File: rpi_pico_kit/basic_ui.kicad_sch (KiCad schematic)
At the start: 40 parts, among them SW2 RotaryEncoder_Switch, SW3 SW_Push, SW4 SW_Push, SW5 SW_Push, SW6 SW_Push, U11 74HC14, U5 74HC14

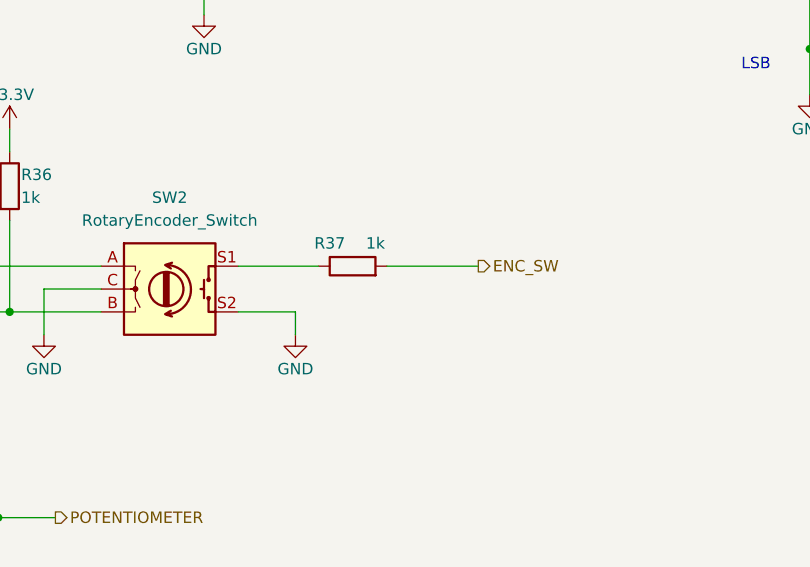
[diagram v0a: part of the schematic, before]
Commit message: changed encoder button pull-up to pull-down
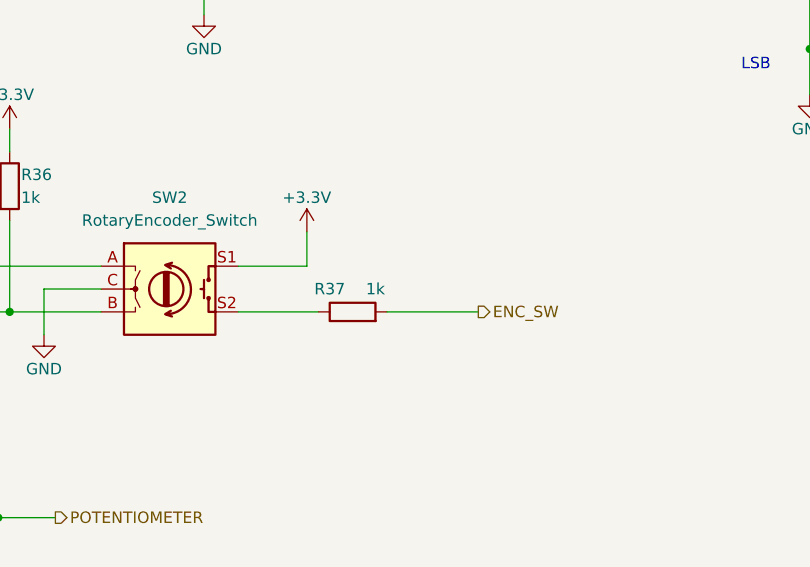
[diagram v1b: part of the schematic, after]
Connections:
- net +3V3: now also SW2.S1
- net GND: no longer SW2.S2
- net at R37.1: now also SW2.S2; no longer SW2.S1
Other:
- moved on the sheet: R37
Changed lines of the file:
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@@
+    (stroke (width 0) (type default))
+  )
+  (wire (pts (xy 92.71 142.24) (xy 92.71 138.43))
     (stroke (width 0) (type default))
   )
@@
     (stroke (width 0) (type default))
   )
-  (wire (pts (xy 85.09 142.24) (xy 93.98 142.24))
-    (stroke (width 0) (type default))
-  )
   (wire (pts (xy 227.33 129.54) (xy 227.33 130.81))
     (stroke (width 0) (type default))
@@
     (stroke (width 0) (type default))
   )
-  (wire (pts (xy 91.44 147.32) (xy 91.44 149.86))
-    (stroke (width 0) (type default))
-  )
   (wire (pts (xy 240.03 92.71) (xy 240.03 121.92))
     (stroke (width 0) (type default))
@@
     (stroke (width 0) (type default))
   )
+  (wire (pts (xy 85.09 142.24) (xy 92.71 142.24))
+    (stroke (width 0) (type default))
+  )
   (wire (pts (xy 48.26 147.32) (xy 59.69 147.32))
     (stroke (width 0) (type default))
@@
     (stroke (width 0) (type default))
   )
-  (wire (pts (xy 85.09 147.32) (xy 91.44 147.32))
-    (stroke (width 0) (type default))
-  )
   (wire (pts (xy 63.5 144.78) (xy 63.5 149.86))
     (stroke (width 0) (type default))
@@
     (stroke (width 0) (type default))
   )
+  (wire (pts (xy 85.09 147.32) (xy 93.98 147.32))
+    (stroke (width 0) (type default))
+  )
   (wire (pts (xy 101.6 99.06) (xy 101.6 101.6))
     (stroke (width 0) (type default))
@@
     (stroke (width 0) (type default))
   )
-  (wire (pts (xy 101.6 142.24) (xy 111.76 142.24))
+  (wire (pts (xy 101.6 147.32) (xy 111.76 147.32))
     (stroke (width 0) (type default))
   )
@@
     (effects (font (size 1.27 1.27)) (justify right))
   )
-  (hierarchical_label "ENC_SW" (shape output) (at 111.76 142.24 0) (fields_autoplaced)
+  (hierarchical_label "ENC_SW" (shape output) (at 111.76 147.32 0) (fields_autoplaced)
     (effects (font (size 1.27 1.27)) (justify left))
   )
@@
     (pin "2")
   )
-  (symbol (lib_id "power:GND") (at 91.44 149.86 0) (unit 1)
-    (in_bom yes) (on_board yes)
-    (property "Reference" "#PWR056" (id 0) (at 91.44 156.21 0)
-      (effects (font (size 1.27 1.27)) hide)
-    )
-    (property "Value" "GND" (id 1) (at 91.44 153.67 0)
-      (effects (font (size 1.27 1.27)))
-    )
-    (property "Footprint" "" (id 2) (at 91.44 149.86 0)
-      (effects (font (size 1.27 1.27)) hide)
-    )
-    (property "Datasheet" "" (id 3) (at 91.44 149.86 0)
-      (effects (font (size 1.27 1.27)) hide)
-    )
-    (pin "1")
-  )
   (symbol (lib_id "power:+3.3V") (at 59.69 127 0) (unit 1)
     (in_bom yes) (on_board yes)
@@
     (pin "2")
   )
-  (symbol (lib_id "Device:R") (at 97.79 142.24 90) (unit 1)
-    (in_bom yes) (on_board yes)
-    (property "Reference" "R37" (id 0) (at 95.25 139.7 90)
-      (effects (font (size 1.27 1.27)))
-    )
-    (property "Value" "1k" (id 1) (at 100.33 139.7 90)
-      (effects (font (size 1.27 1.27)))
-    )
-    (property "Footprint" "Resistor_SMD:R_0805_2012Metric_Pad1.20x1.40mm_HandSolder" (id 2) (at 97.79 144.018 90)
-      (effects (font (size 1.27 1.27)) hide)
-    )
-    (property "Datasheet" "~" (id 3) (at 97.79 142.24 0)
+  (symbol (lib_id "Device:R") (at 97.79 147.32 90) (unit 1)
+    (in_bom yes) (on_board yes)
+    (property "Reference" "R37" (id 0) (at 95.25 144.78 90)
+      (effects (font (size 1.27 1.27)))
+    )
+    (property "Value" "1k" (id 1) (at 100.33 144.78 90)
+      (effects (font (size 1.27 1.27)))
+    )
+    (property "Footprint" "Resistor_SMD:R_0805_2012Metric_Pad1.20x1.40mm_HandSolder" (id 2) (at 97.79 149.098 90)
+      (effects (font (size 1.27 1.27)) hide)
+    )
+    (property "Datasheet" "~" (id 3) (at 97.79 147.32 0)
       (effects (font (size 1.27 1.27)) hide)
     )
@@
       (effects (font (size 1.27 1.27)) hide)
     )
+    (pin "1")
+  )
+  (symbol (lib_id "power:+3.3V") (at 92.71 138.43 0) (unit 1)
+    (in_bom yes) (on_board yes)
+    (property "Reference" "#PWR?" (id 0) (at 92.71 142.24 0)
+      (effects (font (size 1.27 1.27)) hide)
+    )
+    (property "Value" "+3.3V" (id 1) (at 92.71 134.62 0)
+      (effects (font (size 1.27 1.27)))
+    )
+    (property "Footprint" "" (id 2) (at 92.71 138.43 0)
+      (effects (font (size 1.27 1.27)) hide)
+    )
+    (property "Datasheet" "" (id 3) (at 92.71 138.43 0)
+      (effects (font (size 1.27 1.27)) hide)
+    )

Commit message: added some footprints
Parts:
- D10, D11, D12, D9: footprint LED_SMD:LED_1206_3216Metric_Pad1.42x1.75mm_HandSolder -> LED_SMD:LED_0805_2012Metric_Pad1.15x1.40mm_HandSolder
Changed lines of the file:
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@@
       (effects (font (size 1.27 1.27)) (justify right))
     )
-    (property "Footprint" "LED_SMD:LED_1206_3216Metric_Pad1.42x1.75mm_HandSolder" (id 2) (at 101.6 41.91 0)
+    (property "Footprint" "LED_SMD:LED_0805_2012Metric_Pad1.15x1.40mm_HandSolder" (id 2) (at 101.6 41.91 0)
       (effects (font (size 1.27 1.27)) hide)
     )
@@
       (effects (font (size 1.27 1.27)) (justify right))
     )
-    (property "Footprint" "LED_SMD:LED_1206_3216Metric_Pad1.42x1.75mm_HandSolder" (id 2) (at 49.53 95.25 0)
+    (property "Footprint" "LED_SMD:LED_0805_2012Metric_Pad1.15x1.40mm_HandSolder" (id 2) (at 49.53 95.25 0)
       (effects (font (size 1.27 1.27)) hide)
     )
@@
   (symbol (lib_id "power:+3.3V") (at 92.71 138.43 0) (unit 1)
     (in_bom yes) (on_board yes)
-    (property "Reference" "#PWR?" (id 0) (at 92.71 142.24 0)
+    (property "Reference" "#PWR03" (id 0) (at 92.71 142.24 0)
       (effects (font (size 1.27 1.27)) hide)
     )
@@
       (effects (font (size 1.27 1.27)) (justify right))
     )
-    (property "Footprint" "LED_SMD:LED_1206_3216Metric_Pad1.42x1.75mm_HandSolder" (id 2) (at 101.6 95.25 0)
+    (property "Footprint" "LED_SMD:LED_0805_2012Metric_Pad1.15x1.40mm_HandSolder" (id 2) (at 101.6 95.25 0)
       (effects (font (size 1.27 1.27)) hide)
     )
@@
       (effects (font (size 1.27 1.27)) (justify right))
     )
-    (property "Footprint" "LED_SMD:LED_1206_3216Metric_Pad1.42x1.75mm_HandSolder" (id 2) (at 49.53 41.91 0)
-      (effects (font (size 1.27 1.27)) hide)
-    )
+    (property "Footprint" "LED_SMD:LED_0805_2012Metric_Pad1.15x1.40mm_HandSolder" (id 2) (at 49.53 41.91 0)
+      (effects (font (size 1.27 1.27)) hide)
+    )

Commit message: edited 5V I2C, added some footprints, MPNs, added HDMI footprint library
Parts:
- U11: footprint (none) -> Package_SO:SOIC-14_3.9x8.7mm_P1.27mm
- U5: footprint (none) -> Package_SO:SOIC-14_3.9x8.7mm_P1.27mm; Manufacturer Part Number (none) -> 74HC14S14-13; Supplier (none) -> Digikey; Supplier Part URL (none) -> https://www.digikey.cz/en/products/detail/diodes-incorporat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
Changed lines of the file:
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@@
       (effects (font (size 1.27 1.27)))
     )
-    (property "Footprint" "" (id 2) (at 200.66 92.71 0)
+    (property "Footprint" "Package_SO:SOIC-14_3.9x8.7mm_P1.27mm" (id 2) (at 200.66 92.71 0)
       (effects (font (size 1.27 1.27)) hide)
     )
     (property "Datasheet" "http://www.ti.com/lit/gpn/sn74HC14" (id 3) (at 200.66 92.71 0)
+      (effects (font (size 1.27 1.27)) hide)
+    )
+    (property "Manufacturer Part Number" "74HC14S14-13" (id 4) (at 91.44 101.6 0)
+      (effects (font (size 1.27 1.27)) hide)
+    )
+    (property "Supplier" "Digikey" (id 5) (at 91.44 101.6 0)
+      (effects (font (size 1.27 1.27)) hide)
+    )
+    (property "Supplier Part URL" "https://www.digikey.cz/en/products/detail/diodes-incorporated/74HC14S14-13/4249403" (id 6) (at 91.44 101.6 0)
       (effects (font (size 1.27 1.27)) hide)
     )
@@
       (effects (font (size 1.27 1.27)))
     )
-    (property "Footprint" "" (id 2) (at 39.37 48.26 0)
+    (property "Footprint" "Package_SO:SOIC-14_3.9x8.7mm_P1.27mm" (id 2) (at 39.37 48.26 0)
       (effects (font (size 1.27 1.27)) hide)
     )
@@
       (effects (font (size 1.27 1.27)))
     )
-    (property "Footprint" "" (id 2) (at 39.37 101.6 0)
+    (property "Footprint" "Package_SO:SOIC-14_3.9x8.7mm_P1.27mm" (id 2) (at 39.37 101.6 0)
       (effects (font (size 1.27 1.27)) hide)
     )
     (property "Datasheet" "http://www.ti.com/lit/gpn/sn74HC14" (id 3) (at 39.37 101.6 0)
+      (effects (font (size 1.27 1.27)) hide)
+    )
+    (property "Manufacturer Part Number" "74HC14S14-13" (id 4) (at 91.44 101.6 0)
+      (effects (font (size 1.27 1.27)) hide)
+    )
+    (property "Supplier" "Digikey" (id 5) (at 91.44 101.6 0)
+      (effects (font (size 1.27 1.27)) hide)
+    )
+    (property "Supplier Part URL" "https://www.digikey.cz/en/products/detail/diodes-incorporated/74HC14S14-13/4249403" (id 6) (at 91.44 101.6 0)
       (effects (font (size 1.27 1.27)) hide)
     )
@@
       (effects (font (size 1.27 1.27)))
     )
-    (property "Footprint" "" (id 2) (at 200.66 118.11 0)
+    (property "Footprint" "Package_SO:SOIC-14_3.9x8.7mm_P1.27mm" (id 2) (at 200.66 118.11 0)
       (effects (font (size 1.27 1.27)) hide)
     )
     (property "Datasheet" "http://www.ti.com/lit/gpn/sn74HC14" (id 3) (at 200.66 118.11 0)
+      (effects (font (size 1.27 1.27)) hide)
+    )
+    (property "Manufacturer Part Number" "74HC14S14-13" (id 4) (at 91.44 101.6 0)
+      (effects (font (size 1.27 1.27)) hide)
+    )
+    (property "Supplier" "Digikey" (id 5) (at 91.44 101.6 0)
+      (effects (font (size 1.27 1.27)) hide)
+    )
+    (property "Supplier Part URL" "https://www.digikey.cz/en/products/detail/diodes-incorporated/74HC14S14-13/4249403" (id 6) (at 91.44 101.6 0)
       (effects (font (size 1.27 1.27)) hide)
     )
@@
       (effects (font (size 1.27 1.27)))
     )
-    (property "Footprint" "" (id 2) (at 91.44 48.26 0)
+    (property "Footprint" "Package_SO:SOIC-14_3.9x8.7mm_P1.27mm" (id 2) (at 91.44 48.26 0)
       (effects (font (size 1.27 1.27)) hide)
     )
@@
       (effects (font (size 1.27 1.27)))
     )
-    (property "Footprint" "" (id 2) (at 200.66 105.41 0)
+    (property "Footprint" "Package_SO:SOIC-14_3.9x8.7mm_P1.27mm" (id 2) (at 200.66 105.41 0)
       (effects (font (size 1.27 1.27)) hide)
     )
     (property "Datasheet" "http://www.ti.com/lit/gpn/sn74HC14" (id 3) (at 200.66 105.41 0)
+      (effects (font (size 1.27 1.27)) hide)
+    )
+    (property "Manufacturer Part Number" "74HC14S14-13" (id 4) (at 91.44 101.6 0)
+      (effects (font (size 1.27 1.27)) hide)
+    )
+    (property "Supplier" "Digikey" (id 5) (at 91.44 101.6 0)
+      (effects (font (size 1.27 1.27)) hide)
+    )
+    (property "Supplier Part URL" "https://www.digikey.cz/en/products/detail/diodes-incorporated/74HC14S14-13/4249403" (id 6) (at 91.44 101.6 0)
       (effects (font (size 1.27 1.27)) hide)
     )
@@
       (effects (font (size 1.27 1.27)))
     )
-    (property "Footprint" "" (id 2) (at 200.66 80.01 0)
+    (property "Footprint" "Package_SO:SOIC-14_3.9x8.7mm_P1.27mm" (id 2) (at 200.66 80.01 0)
       (effects (font (size 1.27 1.27)) hide)
     )
     (property "Datasheet" "http://www.ti.com/lit/gpn/sn74HC14" (id 3) (at 200.66 80.01 0)
+      (effects (font (size 1.27 1.27)) hide)
+    )
+    (property "Manufacturer Part Number" "74HC14S14-13" (id 4) (at 91.44 101.6 0)
+      (effects (font (size 1.27 1.27)) hide)
+    )
+    (property "Supplier" "Digikey" (id 5) (at 91.44 101.6 0)
+      (effects (font (size 1.27 1.27)) hide)
+    )
+    (property "Supplier Part URL" "https://www.digikey.cz/en/products/detail/diodes-incorporated/74HC14S14-13/4249403" (id 6) (at 91.44 101.6 0)
       (effects (font (size 1.27 1.27)) hide)
     )
@@
       (effects (font (size 1.27 1.27)))
     )
-    (property "Footprint" "" (id 2) (at 91.44 101.6 0)
+    (property "Footprint" "Package_SO:SOIC-14_3.9x8.7mm_P1.27mm" (id 2) (at 91.44 101.6 0)
       (effects (font (size 1.27 1.27)) hide)
     )
     (property "Datasheet" "http://www.ti.com/lit/gpn/sn74HC14" (id 3) (at 91.44 101.6 0)
+      (effects (font (size 1.27 1.27)) hide)
+    )
+    (property "Manufacturer Part Number" "74HC14S14-13" (id 4) (at 91.44 101.6 0)
+      (effects (font (size 1.27 1.27)) hide)
+    )
+    (property "Supplier" "Digikey" (id 5) (at 91.44 101.6 0)
+      (effects (font (size 1.27 1.27)) hide)
+    )
+    (property "Supplier Part URL" "https://www.digikey.cz/en/products/detail/diodes-incorporated/74HC14S14-13/4249403" (id 6) (at 91.44 101.6 0)
       (effects (font (size 1.27 1.27)) hide)
     )
@@
       (effects (font (size 1.27 1.27)) (justify left))
     )
-    (property "Footprint" "" (id 2) (at 267.97 80.01 0)
+    (property "Footprint" "Package_SO:SOIC-14_3.9x8.7mm_P1.27mm" (id 2) (at 267.97 80.01 0)
       (effects (font (size 1.27 1.27)) hide)
     )
@@
       (effects (font (size 1.27 1.27)) hide)
     )
+    (property "Manufacturer Part Number" "74HC14S14-13" (id 4) (at 91.44 101.6 0)
+      (effects (font (size 1.27 1.27)) hide)
+    )
+    (property "Supplier" "Digikey" (id 5) (at 91.44 101.6 0)
+      (effects (font (size 1.27 1.27)) hide)
+    )
+    (property "Supplier Part URL" "https://www.digikey.cz/en/products/detail/diodes-incorporated/74HC14S14-13/4249403" (id 6) (at 91.44 101.6 0)
+      (effects (font (size 1.27 1.27)) hide)
+    )

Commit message: added some footprints and MPNs
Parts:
- SW2: footprint (none) -> Rotary_Encoder:RotaryEncoder_Alps_EC11E-Switch_Vertical_H20mm; Manufacturer Part Number (none) -> EN11-HSM1BF20; Supplier (none) -> Digikey; Supplier Part URL (none) -> https://www.digikey.cz/en/products/detail/tt-electronics-bi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
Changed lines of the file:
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@@
       (effects (font (size 1.27 1.27)))
     )
-    (property "Footprint" "" (id 2) (at 73.66 140.716 0)
+    (property "Footprint" "Rotary_Encoder:RotaryEncoder_Alps_EC11E-Switch_Vertical_H20mm" (id 2) (at 73.66 140.716 0)
       (effects (font (size 1.27 1.27)) hide)
     )
@@
       (effects (font (size 1.27 1.27)) hide)
     )
+    (property "Manufacturer Part Number" "EN11-HSM1BF20" (id 4) (at 77.47 144.78 0)
+      (effects (font (size 1.27 1.27)) hide)
+    )
+    (property "Supplier" "Digikey" (id 5) (at 77.47 144.78 0)
+      (effects (font (size 1.27 1.27)) hide)
+    )
+    (property "Supplier Part URL" "https://www.digikey.cz/en/products/detail/tt-electronics-bi/EN11-HSM1BF20/2620667" (id 6) (at 77.47 144.78 0)
+      (effects (font (size 1.27 1.27)) hide)
+    )

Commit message: added MPNs for capacitors
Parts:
- C19: Manufacturer Part Number (none) -> C0805C103K5RAC7210; Supplier (none) -> Digikey; Supplier Part URL (none) -> https://www.digikey.cz/en/products/detail/kemet/C0805C103K5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
- C23: Manufacturer Part Number (none) -> C0805C104M3RAC7800; Supplier (none) -> Digikey; Supplier Part URL (none) -> https://www.digikey.cz/en/products/detail/kemet/C0805C104M3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
- RV1: Manufacturer Part Number (none) -> PT01-B125D-B103; Supplier (none) -> Digikey; Supplier Part URL (none) -> https://www.digikey.cz/en/products/detail/cui-devices/PT01-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
- SW3, SW4, SW5, SW6: Manufacturer Part Number (none) -> LA215000; Supplier (none) -> Laskakit; Supplier Part URL (none) -> https://www.laskakit.cz/tlacitko-6x6x5mm/
- U11: Manufacturer Part Number (none) -> 74HC14S14-13; Supplier (none) -> Digikey; Supplier Part URL (none) -> https://www.digikey.cz/en/products/detail/diodes-incorporat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
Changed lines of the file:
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@@
+      (effects (font (size 1.27 1.27)) hide)
+    )
+    (property "Manufacturer Part Number" "LA215000" (id 4) (at 157.48 92.71 0)
+      (effects (font (size 1.27 1.27)) hide)
+    )
+    (property "Supplier" "Laskakit" (id 5) (at 157.48 92.71 0)
+      (effects (font (size 1.27 1.27)) hide)
+    )
+    (property "Supplier Part URL" "https://www.laskakit.cz/tlacitko-6x6x5mm/" (id 6) (at 157.48 92.71 0)
       (effects (font (size 1.27 1.27)) hide)
     )
@@
       (effects (font (size 1.27 1.27)) hide)
     )
+    (property "Manufacturer Part Number" "PT01-B125D-B103" (id 4) (at 38.1 170.18 0)
+      (effects (font (size 1.27 1.27)) hide)
+    )
+    (property "Supplier" "Digikey" (id 5) (at 38.1 170.18 0)
+      (effects (font (size 1.27 1.27)) hide)
+    )
+    (property "Supplier Part URL" "https://www.digikey.cz/en/products/detail/cui-devices/PT01-B125D-B103/15903924" (id 6) (at 38.1 170.18 0)
+      (effects (font (size 1.27 1.27)) hide)
+    )
     (pin "1")
     (pin "2")
@@
       (effects (font (size 1.27 1.27)) hide)
     )
+    (property "Manufacturer Part Number" "C0805C103K5RAC7210" (id 4) (at 58.42 177.8 0)
+      (effects (font (size 1.27 1.27)) hide)
+    )
+    (property "Supplier" "Digikey" (id 5) (at 58.42 177.8 0)
+      (effects (font (size 1.27 1.27)) hide)
+    )
+    (property "Supplier Part URL" "https://www.digikey.cz/en/products/detail/kemet/C0805C103K5RAC7210/3317006" (id 6) (at 58.42 177.8 0)
+      (effects (font (size 1.27 1.27)) hide)
+    )
     (pin "1")
     (pin "2")
@@
     )
     (property "Datasheet" "http://www.ti.com/lit/gpn/sn74HC14" (id 3) (at 39.37 48.26 0)
+      (effects (font (size 1.27 1.27)) hide)
+    )
+    (property "Manufacturer Part Number" "74HC14S14-13" (id 4) (at 39.37 48.26 0)
+      (effects (font (size 1.27 1.27)) hide)
+    )
+    (property "Supplier" "Digikey" (id 5) (at 39.37 48.26 0)
+      (effects (font (size 1.27 1.27)) hide)
+    )
+    (property "Supplier Part URL" "https://www.digikey.cz/en/products/detail/diodes-incorporated/74HC14S14-13/4249403" (id 6) (at 39.37 48.26 0)
       (effects (font (size 1.27 1.27)) hide)
     )
@@
       (effects (font (size 1.27 1.27)) hide)
     )
+    (property "Manufacturer Part Number" "LA215000" (id 4) (at 157.48 105.41 0)
+      (effects (font (size 1.27 1.27)) hide)
+    )
+    (property "Supplier" "Laskakit" (id 5) (at 157.48 105.41 0)
+      (effects (font (size 1.27 1.27)) hide)
+    )
+    (property "Supplier Part URL" "https://www.laskakit.cz/tlacitko-6x6x5mm/" (id 6) (at 157.48 105.41 0)
+      (effects (font (size 1.27 1.27)) hide)
+    )
     (pin "1")
     (pin "2")
@@
     )
     (property "Datasheet" "~" (id 3) (at 157.48 113.03 0)
+      (effects (font (size 1.27 1.27)) hide)
+    )
+    (property "Manufacturer Part Number" "LA215000" (id 4) (at 157.48 118.11 0)
+      (effects (font (size 1.27 1.27)) hide)
+    )
+    (property "Supplier" "Laskakit" (id 5) (at 157.48 118.11 0)
+      (effects (font (size 1.27 1.27)) hide)
+    )
+    (property "Supplier Part URL" "https://www.laskakit.cz/tlacitko-6x6x5mm/" (id 6) (at 157.48 118.11 0)
       (effects (font (size 1.27 1.27)) hide)
     )
@@
       (effects (font (size 1.27 1.27)) hide)
     )
+    (property "Manufacturer Part Number" "74HC14S14-13" (id 4) (at 91.44 48.26 0)
+      (effects (font (size 1.27 1.27)) hide)
+    )
+    (property "Supplier" "Digikey" (id 5) (at 91.44 48.26 0)
+      (effects (font (size 1.27 1.27)) hide)
+    )
+    (property "Supplier Part URL" "https://www.digikey.cz/en/products/detail/diodes-incorporated/74HC14S14-13/4249403" (id 6) (at 91.44 48.26 0)
+      (effects (font (size 1.27 1.27)) hide)
+    )
     (pin "12")
     (pin "13")
@@
     )
     (property "Datasheet" "~" (id 3) (at 256.54 69.85 0)
+      (effects (font (size 1.27 1.27)) hide)
+    )
+    (property "Manufacturer Part Number" "C0805C104M3RAC7800" (id 4) (at 256.54 69.85 0)
+      (effects (font (size 1.27 1.27)) hide)
+    )
+    (property "Supplier" "Digikey" (id 5) (at 256.54 69.85 0)
+      (effects (font (size 1.27 1.27)) hide)
+    )
+    (property "Supplier Part URL" "https://www.digikey.cz/en/products/detail/kemet/C0805C104M3RAC7800/2211748" (id 6) (at 256.54 69.85 0)
       (effects (font (size 1.27 1.27)) hide)
     )
@@
       (effects (font (size 1.27 1.27)) hide)
     )
+    (property "Manufacturer Part Number" "LA215000" (id 4) (at 157.48 80.01 0)
+      (effects (font (size 1.27 1.27)) hide)
+    )
+    (property "Supplier" "Laskakit" (id 5) (at 157.48 80.01 0)
+      (effects (font (size 1.27 1.27)) hide)
+    )
+    (property "Supplier Part URL" "https://www.laskakit.cz/tlacitko-6x6x5mm/" (id 6) (at 157.48 80.01 0)
+      (effects (font (size 1.27 1.27)) hide)
+    )

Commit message: added MPNs for resistors
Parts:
- R20, R23, R26, R29, R33, R34, R35, R36, R37, R57, R58, R59, R60, R63, R90, R92: Manufacturer Part Number (none) -> RC0805FR-071KL; Supplier (none) -> Digikey; Supplier Part URL (none) -> https://www.digikey.cz/en/products/detail/yageo/RC0805FR-07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
- R22, R25, R28, R31: Manufacturer Part Number (none) -> RC0805FR-0710KL; Supplier (none) -> Digikey; Supplier Part URL (none) -> https://www.digikey.cz/en/products/detail/yageo/RC0805FR-07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
- R32: Manufacturer Part Number (none) -> RC0805FR-07100RL; Supplier (none) -> Digikey; Supplier Part URL (none) -> https://www.digikey.cz/en/products/detail/yageo/RC0805FR-07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
- R61, R62, R64, R91, R93: Manufacturer Part Number (none) -> RC0805FR-072KL; Supplier (none) -> Digikey; Supplier Part URL (none) -> https://www.digikey.cz/en/products/detail/yageo/RC0805FR-07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
